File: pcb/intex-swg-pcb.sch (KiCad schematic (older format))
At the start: 10 parts, among them J1 230V, J2 Relay Board, J3 Display Board, J4 Main Board, J5 5V_INTEX Pin Select, J6 GND Pin Select

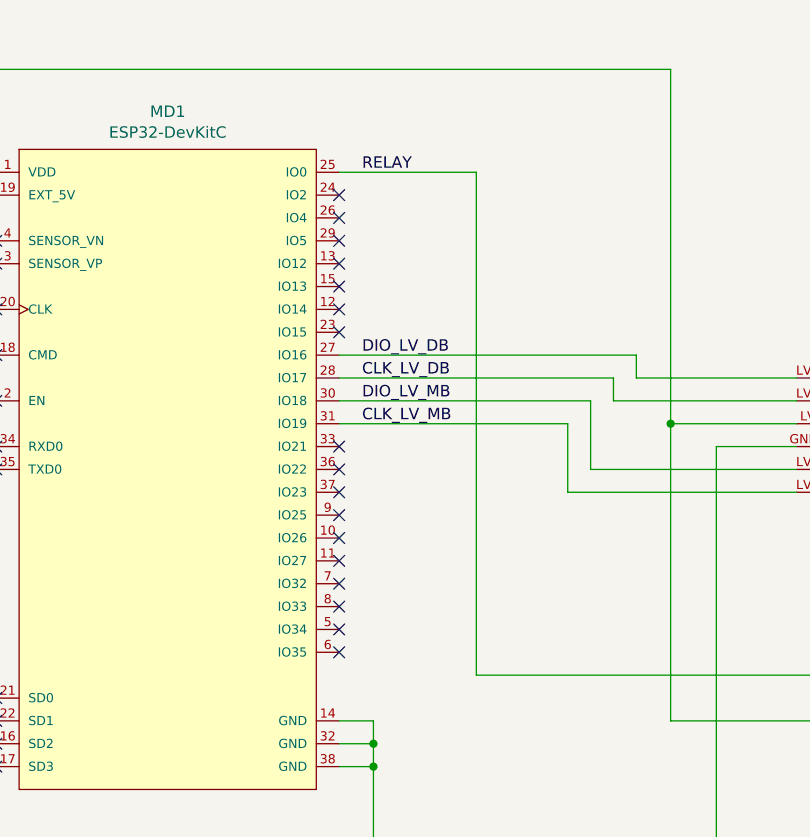
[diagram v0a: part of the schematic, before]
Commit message: Swapped relay to GPIO2
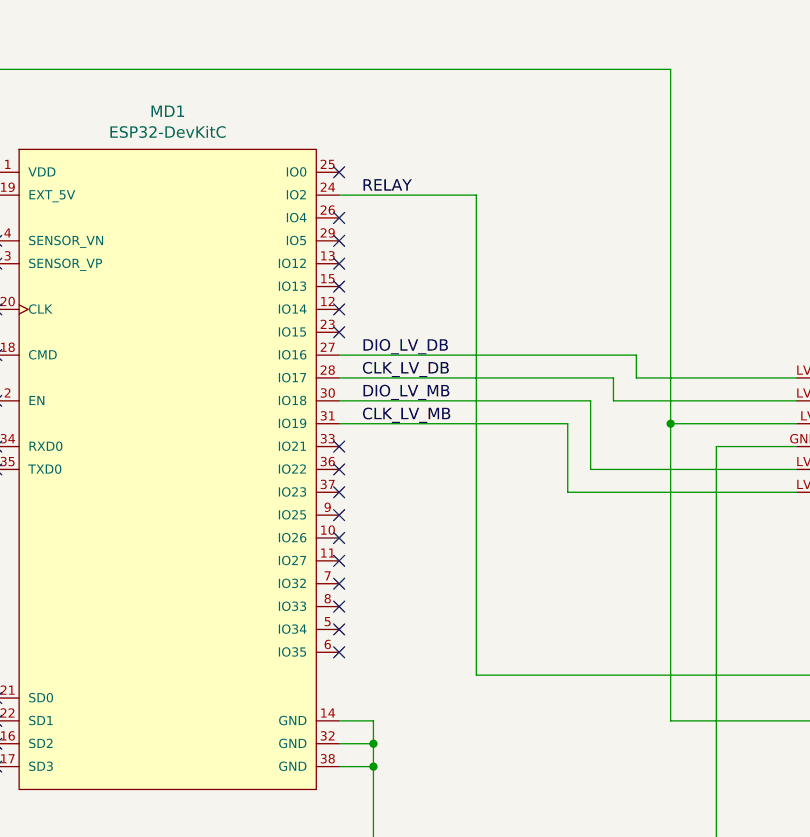
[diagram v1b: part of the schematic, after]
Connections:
- net RELAY: now also MD1.24 (IO2); no longer MD1.25 (IO0)
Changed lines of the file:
@@
 Sheet 1 1
 Title "Intex SWG with jumpers"
-Date "2022-05-22"
-Rev "3.0"
+Date "2022-06-06"
+Rev "3.1"
 Comp ""
 Comment1 ""
@@
 Wire Wire Line
 	10150 4500 6150 4500
-Wire Wire Line
-	5300 2100 5300 4300
-Wire Wire Line
-	5300 2100 4700 2100
 Wire Wire Line
 	4700 3000 5900 3000
@@
 Wire Wire Line
 	1100 3400 1100 3300
-NoConn ~ 4700 2200
 NoConn ~ 4700 2300
 NoConn ~ 4700 2400
@@
 Wire Wire Line
 	1800 1800 1800 1550
-Text Label 4800 2100 0    50   ~ 0
-RELAY
 Wire Wire Line
 	3200 2200 2750 2200
@@
 Wire Wire Line
 	8400 3900 8400 5050
+Text Label 4800 2200 0    50   ~ 0
+RELAY
+Wire Wire Line
+	5300 2200 4700 2200
+Wire Wire Line
+	5300 2200 5300 4300
+NoConn ~ 4700 2100
 $EndSCHEMATC
